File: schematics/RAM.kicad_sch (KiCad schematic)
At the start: 17 parts, among them U36 CY62256-70PC

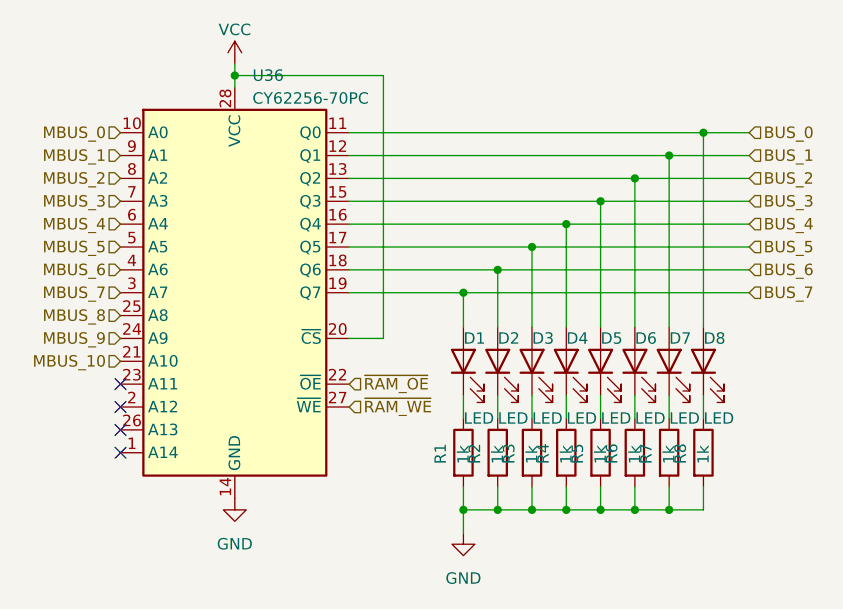
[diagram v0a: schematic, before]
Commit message: control logic finished
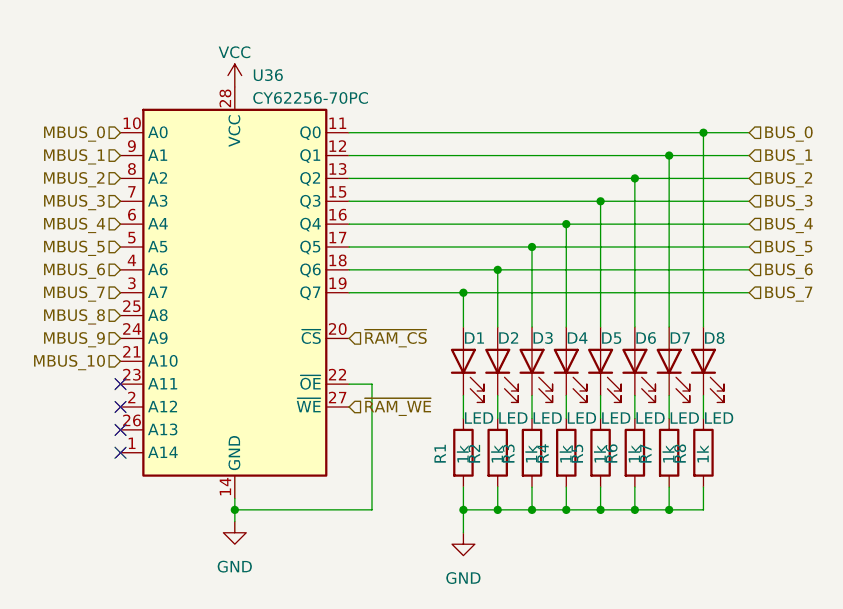
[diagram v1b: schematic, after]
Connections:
- net ~{RAM_OE} is gone; now on net GND: U36.22 (~{OE})
- net VCC: no longer U36.20 (~{CS})
- new net ~{RAM_CS}: U36.20 (~{CS})
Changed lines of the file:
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@@
   (junction (at 173.99 120.65) (diameter 0) (color 0 0 0 0)
   )
-  (junction (at 137.16 72.39) (diameter 0) (color 0 0 0 0)
-  )
   (junction (at 170.18 120.65) (diameter 0) (color 0 0 0 0)
   )
@@
   )
   (junction (at 185.42 81.28) (diameter 0) (color 0 0 0 0)
+  )
+  (junction (at 137.16 120.65) (diameter 0) (color 0 0 0 0)
   )
   (junction (at 181.61 120.65) (diameter 0) (color 0 0 0 0)
@@
     (stroke (width 0) (type default))
   )
-  (wire (pts (xy 153.67 72.39) (xy 153.67 101.6))
-    (stroke (width 0) (type default))
-  )
   (wire (pts (xy 177.8 86.36) (xy 177.8 100.33))
     (stroke (width 0) (type default))
   )
+  (wire (pts (xy 152.4 120.65) (xy 152.4 106.68))
+    (stroke (width 0) (type default))
+  )
   (wire (pts (xy 170.18 118.11) (xy 170.18 120.65))
     (stroke (width 0) (type default))
@@
     (stroke (width 0) (type default))
   )
-  (wire (pts (xy 137.16 71.12) (xy 137.16 72.39))
-    (stroke (width 0) (type default))
-  )
   (wire (pts (xy 170.18 107.95) (xy 170.18 110.49))
     (stroke (width 0) (type default))
@@
     (stroke (width 0) (type default))
   )
-  (wire (pts (xy 137.16 72.39) (xy 153.67 72.39))
-    (stroke (width 0) (type default))
-  )
   (wire (pts (xy 149.86 86.36) (xy 177.8 86.36))
     (stroke (width 0) (type default))
@@
     (stroke (width 0) (type default))
   )
+  (wire (pts (xy 152.4 106.68) (xy 149.86 106.68))
+    (stroke (width 0) (type default))
+  )
   (wire (pts (xy 177.8 120.65) (xy 181.61 120.65))
     (stroke (width 0) (type default))
@@
     (stroke (width 0) (type default))
   )
+  (wire (pts (xy 137.16 120.65) (xy 137.16 119.38))
+    (stroke (width 0) (type default))
+  )
   (wire (pts (xy 149.86 83.82) (xy 181.61 83.82))
     (stroke (width 0) (type default))
@@
     (stroke (width 0) (type default))
   )
+  (wire (pts (xy 137.16 121.92) (xy 137.16 120.65))
+    (stroke (width 0) (type default))
+  )
   (wire (pts (xy 185.42 81.28) (xy 185.42 100.33))
     (stroke (width 0) (type default))
@@
     (stroke (width 0) (type default))
   )
-  (wire (pts (xy 137.16 72.39) (xy 137.16 73.66))
-    (stroke (width 0) (type default))
-  )
   (wire (pts (xy 173.99 118.11) (xy 173.99 120.65))
     (stroke (width 0) (type default))
@@
     (stroke (width 0) (type default))
   )
-  (wire (pts (xy 153.67 101.6) (xy 149.86 101.6))
+  (wire (pts (xy 137.16 120.65) (xy 152.4 120.65))
     (stroke (width 0) (type default))
   )
@@
     (effects (font (size 1.27 1.27)) (justify left))
   )
-  (hierarchical_label "~{RAM_OE}" (shape input) (at 149.86 106.68 0) (fields_autoplaced)
+  (hierarchical_label "~{RAM_CS}" (shape input) (at 149.86 101.6 0) (fields_autoplaced)
     (effects (font (size 1.27 1.27)) (justify left))
   )
@@
     )
   )
-  (symbol (lib_id "power:VCC") (at 137.16 71.12 0) (unit 1)
-    (in_bom yes) (on_board yes) (dnp no) (fields_autoplaced)
-    (property "Reference" "#PWR074" (at 137.16 74.93 0)
-      (effects (font (size 1.27 1.27)) hide)
-    )
-    (property "Value" "VCC" (at 137.16 67.31 0)
+  (symbol (lib_id "power:VCC") (at 137.16 73.66 0) (unit 1)
+    (in_bom yes) (on_board yes) (dnp no) (fields_autoplaced)
+    (property "Reference" "#PWR074" (at 137.16 77.47 0)
+      (effects (font (size 1.27 1.27)) hide)
+    )
+    (property "Value" "VCC" (at 137.16 69.85 0)
       (effects (font (size 1.27 1.27)))
     )
-    (property "Footprint" "" (at 137.16 71.12 0)
-      (effects (font (size 1.27 1.27)) hide)
-    )
-    (property "Datasheet" "" (at 137.16 71.12 0)
+    (property "Footprint" "" (at 137.16 73.66 0)
+      (effects (font (size 1.27 1.27)) hide)
+    )
+    (property "Datasheet" "" (at 137.16 73.66 0)
       (effects (font (size 1.27 1.27)) hide)
     )
@@
     )
   )
-  (symbol (lib_id "power:GND") (at 137.16 119.38 0) (unit 1)
-    (in_bom yes) (on_board yes) (dnp no) (fields_autoplaced)
-    (property "Reference" "#PWR03" (at 137.16 125.73 0)
-      (effects (font (size 1.27 1.27)) hide)
-    )
-    (property "Value" "GND" (at 137.16 124.46 0)
+  (symbol (lib_id "power:GND") (at 137.16 121.92 0) (unit 1)
+    (in_bom yes) (on_board yes) (dnp no) (fields_autoplaced)
+    (property "Reference" "#PWR03" (at 137.16 128.27 0)
+      (effects (font (size 1.27 1.27)) hide)
+    )
+    (property "Value" "GND" (at 137.16 127 0)
       (effects (font (size 1.27 1.27)))
     )
-    (property "Footprint" "" (at 137.16 119.38 0)
-      (effects (font (size 1.27 1.27)) hide)
-    )
-    (property "Datasheet" "" (at 137.16 119.38 0)
-      (effects (font (size 1.27 1.27)) hide)
-    )
+    (property "Footprint" "" (at 137.16 121.92 0)
+      (effects (font (size 1.27 1.27)) hide)
+    )
+    (property "Datasheet" "" (at 137.16 121.92 0)
+      (effects (font (size 1.27 1.27)) hide)
+    )
